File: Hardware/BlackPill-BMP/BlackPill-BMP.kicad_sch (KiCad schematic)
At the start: 27 parts, among them J1 VCC, J2 VCC, J3 Conn_01x10, J4 Conn_01x11, J5 GDB_COMM, J6 VCC, J7 GND, J8 JTAG, J9 LogicAna, U1 STM32F411 BlackPill

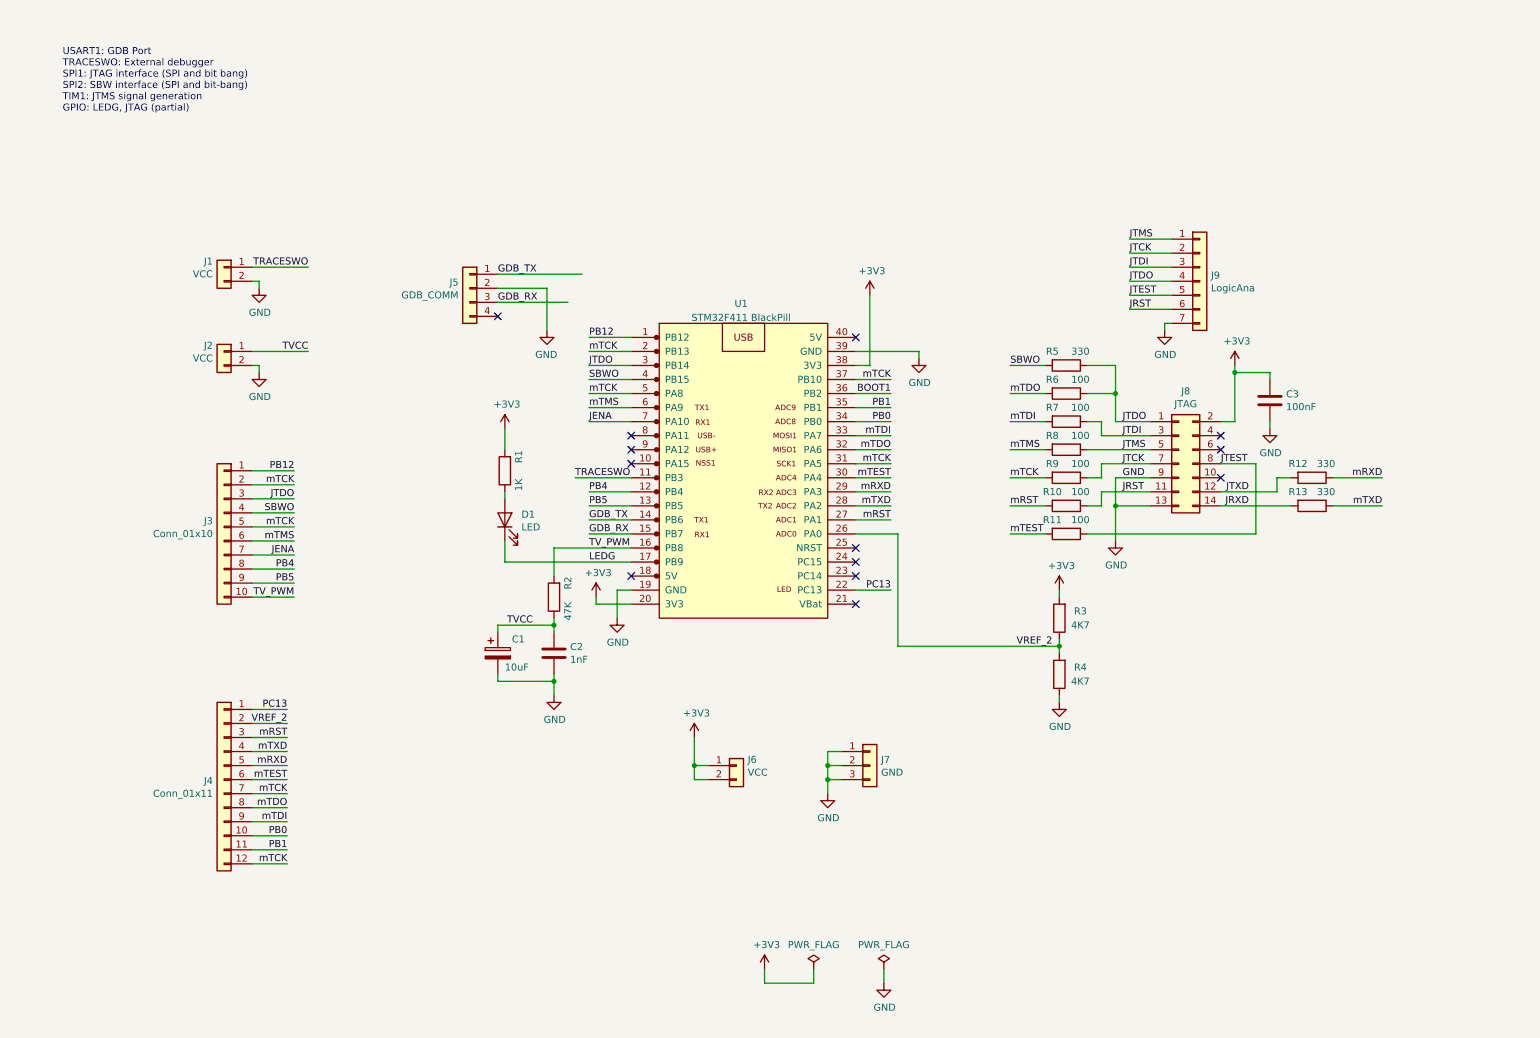
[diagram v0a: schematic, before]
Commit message: Improved BlackPill Board to support both BluePill and BlackPill. Support for variable target voltage.
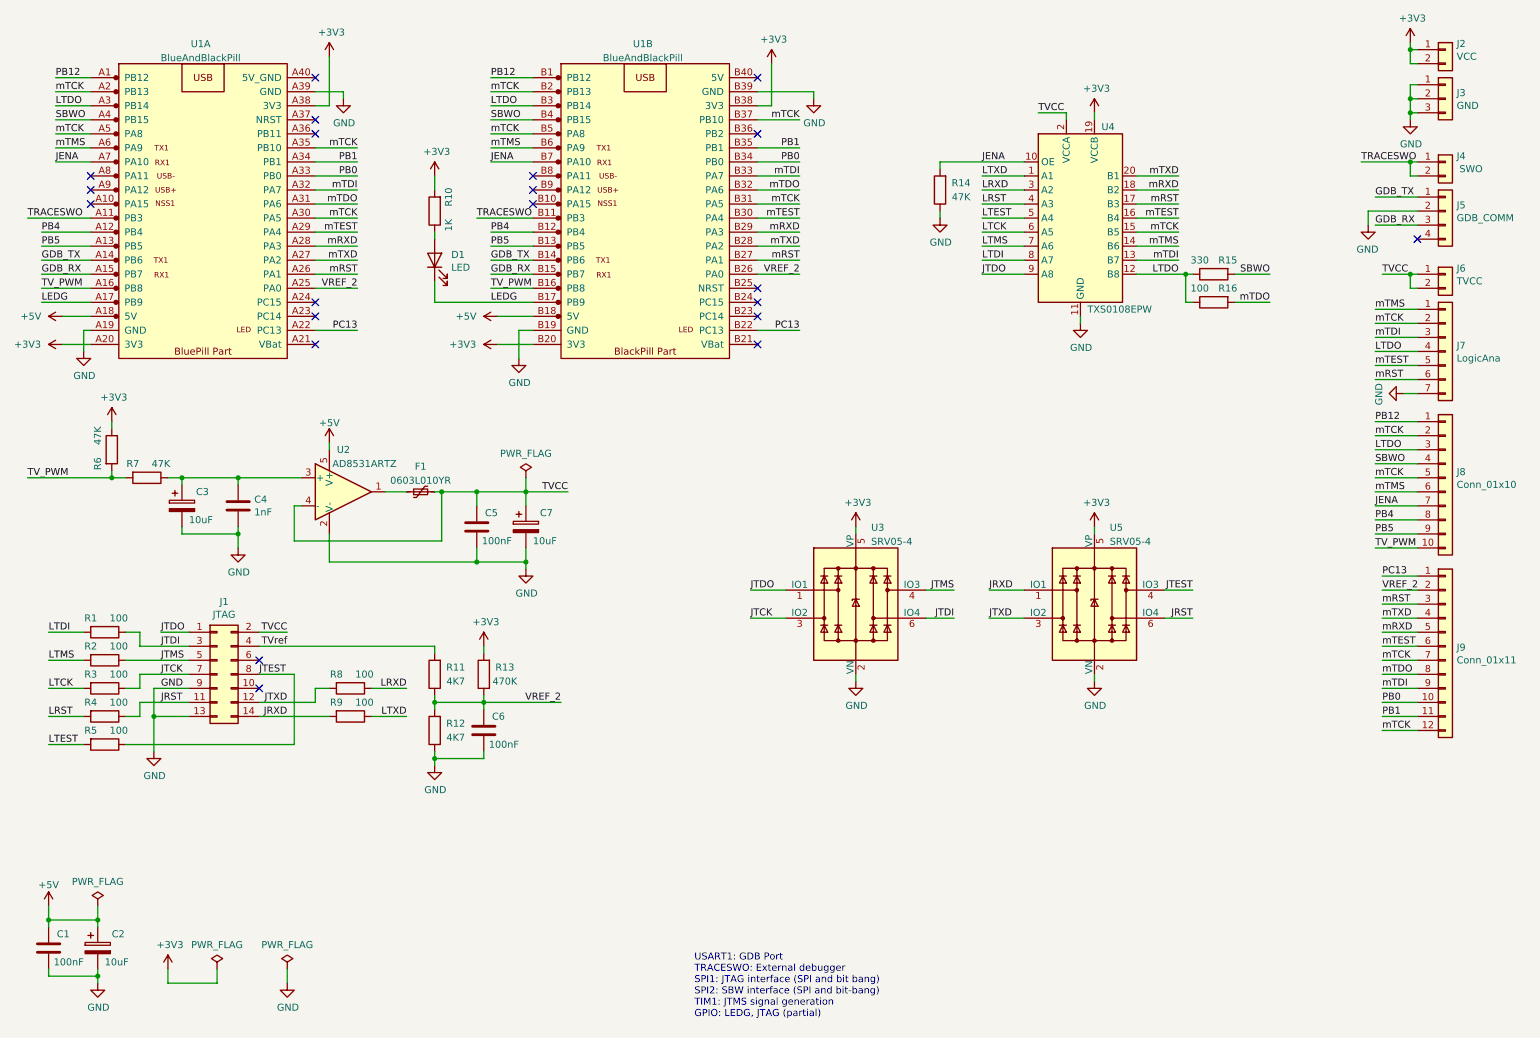
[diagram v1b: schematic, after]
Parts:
- removed U1: STM32F411 BlackPill, lib:BlackPill_F411, symbol BlackPill_F411:BlackPill_F411
- added C1, C6: 100nF, Capacitor_SMD:C_0603_1608Metric_Pad1.08x0.95mm_HandSolder, symbol Device:C
- added C2, C7: 10uF, Capacitor_SMD:C_0603_1608Metric_Pad1.08x0.95mm_HandSolder, symbol Device:C_Polarized
- added F1: 0603L010YR, Fuse:Fuse_0603_1608Metric_Pad1.05x0.95mm_HandSolder, symbol Device:Polyfuse_Small
- added R13: 470K, Resistor_SMD:R_0603_1608Metric_Pad0.98x0.95mm_HandSolder, symbol Device:R
- added R14, R6: 47K, Resistor_SMD:R_0603_1608Metric_Pad0.98x0.95mm_HandSolder, symbol Device:R
- added U1: BlueAndBlackPill, lib:BlueBlackPill, symbol BlueBlackPill:BlueAndBlackPill
- added U2: AD8531ARTZ, Package_TO_SOT_SMD:SOT-23-5_HandSoldering, symbol ad8531artz:AD8531ARTZ
- added U3, U5: SRV05-4, Package_TO_SOT_SMD:SOT-23-6, symbol Power_Protection:SRV05-4
- added U4: TXS0108EPW, Package_SO:TSSOP-20_4.4x6.5mm_P0.65mm, symbol Logic_LevelTranslator:TXS0108EPW
- C3: renamed from C1; footprint Capacitor_THT:CP_Radial_D5.0mm_P2.00mm -> Capacitor_SMD:C_0603_1608Metric_Pad1.08x0.95mm_HandSolder
- C4: renamed from C2; footprint Capacitor_THT:C_Disc_D4.3mm_W1.9mm_P5.00mm -> Capacitor_SMD:C_0603_1608Metric_Pad1.08x0.95mm_HandSolder
- C5: renamed from C3; footprint Capacitor_THT:C_Disc_D4.3mm_W1.9mm_P5.00mm -> Capacitor_SMD:C_0603_1608Metric_Pad1.08x0.95mm_HandSolder
- J4: renamed from J1; value VCC -> SWO
- J6: renamed from J2; value VCC -> TVCC
- R1: renamed from R7; footprint Resistor_THT:R_Axial_DIN0204_L3.6mm_D1.6mm_P7.62mm_Horizontal -> Resistor_SMD:R_0603_1608Metric_Pad0.98x0.95mm_HandSolder
- R10: renamed from R1; footprint Resistor_THT:R_Axial_DIN0204_L3.6mm_D1.6mm_P7.62mm_Horizontal -> Resistor_SMD:R_0603_1608Metric_Pad0.98x0.95mm_HandSolder
- R11: renamed from R3; footprint Resistor_THT:R_Axial_DIN0204_L3.6mm_D1.6mm_P7.62mm_Horizontal -> Resistor_SMD:R_0603_1608Metric_Pad0.98x0.95mm_HandSolder
- R12: renamed from R4; footprint Resistor_THT:R_Axial_DIN0204_L3.6mm_D1.6mm_P7.62mm_Horizontal -> Resistor_SMD:R_0603_1608Metric_Pad0.98x0.95mm_HandSolder
- R15: renamed from R5; footprint Resistor_THT:R_Axial_DIN0204_L3.6mm_D1.6mm_P7.62mm_Horizontal -> Resistor_SMD:R_0603_1608Metric_Pad0.98x0.95mm_HandSolder
- R16: renamed from R6; footprint Resistor_THT:R_Axial_DIN0204_L3.6mm_D1.6mm_P7.62mm_Horizontal -> Resistor_SMD:R_0603_1608Metric_Pad0.98x0.95mm_HandSolder
- R2: renamed from R8; footprint Resistor_THT:R_Axial_DIN0204_L3.6mm_D1.6mm_P7.62mm_Horizontal -> Resistor_SMD:R_0603_1608Metric_Pad0.98x0.95mm_HandSolder
- R3: renamed from R9; footprint Resistor_THT:R_Axial_DIN0204_L3.6mm_D1.6mm_P7.62mm_Horizontal -> Resistor_SMD:R_0603_1608Metric_Pad0.98x0.95mm_HandSolder
- R4: renamed from R10; footprint Resistor_THT:R_Axial_DIN0204_L3.6mm_D1.6mm_P7.62mm_Horizontal -> Resistor_SMD:R_0603_1608Metric_Pad0.98x0.95mm_HandSolder
- R5: renamed from R11; footprint Resistor_THT:R_Axial_DIN0204_L3.6mm_D1.6mm_P7.62mm_Horizontal -> Resistor_SMD:R_0603_1608Metric_Pad0.98x0.95mm_HandSolder
- R7: renamed from R2; footprint Resistor_THT:R_Axial_DIN0204_L3.6mm_D1.6mm_P7.62mm_Horizontal -> Resistor_SMD:R_0603_1608Metric_Pad0.98x0.95mm_HandSolder
- R8: renamed from R12; value 330 -> 100; footprint Resistor_THT:R_Axial_DIN0204_L3.6mm_D1.6mm_P7.62mm_Horizontal -> Resistor_SMD:R_0603_1608Metric_Pad0.98x0.95mm_HandSolder
- R9: renamed from R13; value 330 -> 100; footprint Resistor_THT:R_Axial_DIN0204_L3.6mm_D1.6mm_P7.62mm_Horizontal -> Resistor_SMD:R_0603_1608Metric_Pad0.98x0.95mm_HandSolder
- renumbered J8 to J1, J6 to J2, J7 to J3, J9 to J7, J3 to J8, J4 to J9
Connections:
- net +3V3: now also R13.2, R6.1, U1.A20 (3V3), U1.A38 (3V3), U1.B20 (3V3), U1.B38 (3V3), U3.5 (VP), U4.19 (VCCB), U5.5 (VP); no longer C5.1, J1.2 (Pin_2), R11.2
- net GDB_RX: now also U1.A15 (PB7), U1.B15 (PB7)
- net GDB_TX: now also U1.A14 (PB6), U1.B14 (PB6)
- net GND: now also C5.1, C1.1, C2.2, C6.1, C7.2, R14.1, U1.A19 (GND), U1.A39 (GND), U1.B19 (GND), U1.B39 (GND), U2.2 (V-), U3.2 (VN), U4.11 (GND), U5.2 (VN); no longer C5.2, J4.2 (Pin_2), J6.2 (Pin_2)
- net JENA: now also R14.2, U1.A7 (PA10), U1.B7 (PA10), U4.10 (OE)
- net JRST: now also U5.6 (IO4); no longer J7.6 (Pin_6)
- net JRXD: now also U5.1 (IO1)
- net JTCK: now also U3.3 (IO2); no longer J7.2 (Pin_2)
- net JTDI: now also U3.6 (IO4); no longer J7.3 (Pin_3)
- net JTDO: now also U3.1 (IO1), U4.9 (A8); no longer J7.4 (Pin_4), J8.3 (Pin_3), R15.1, R16.1
- net JTEST: now also U5.4 (IO3); no longer J7.5 (Pin_5)
- net JTMS: now also U3.4 (IO3); no longer J7.1 (Pin_1)
- net JTXD: now also U5.3 (IO2)
- net LEDG: now also U1.A17 (PB9), U1.B17 (PB9)
- net PB0: now also U1.A33 (PB0), U1.B34 (PB0)
- net PB1: now also U1.A34 (PB1), U1.B35 (PB1)
- net PB12: now also U1.A1 (PB12), U1.B1 (PB12)
- net PB4: now also U1.A12 (PB4), U1.B12 (PB4)
- net PB5: now also U1.A13 (PB5), U1.B13 (PB5)
- net PC13: now also U1.A22 (PC13), U1.B22 (PC13)
- net SBWO: now also U1.A4 (PB15), U1.B4 (PB15)
- net TRACESWO: now also J4.2 (Pin_2), U1.A11 (PB3), U1.B11 (PB3)
- net TVCC: now also C5.2, J1.2 (Pin_2), J6.2 (Pin_2), C7.1, F1.2, U2.4 (-), U4.2 (VCCA); no longer C3.1, C4.1, R7.1
- net TV_PWM: now also R6.2, U1.A16 (PB8), U1.B16 (PB8)
- net VREF_2: now also C6.2, R13.1, U1.A25 (PA0), U1.B26 (PA0)
- net mRST: now also J7.6 (Pin_6), U1.A26 (PA1), U1.B27 (PA1), U4.17 (B3); no longer R4.2
- net mRXD: now also U1.A28 (PA3), U1.B29 (PA3), U4.18 (B2); no longer R8.1
- net mTCK: now also J7.2 (Pin_2), U1.A2 (PB13), U1.A30 (PA5), U1.A35 (PB10), U1.A5 (PA8), U1.B2 (PB13), U1.B31 (PA5), U1.B37 (PB10), U1.B5 (PA8), U4.15 (B5); no longer R3.2
- net mTDI: now also J7.3 (Pin_3), U1.A32 (PA7), U1.B33 (PA7), U4.13 (B7); no longer R1.2
- net mTDO: now also U1.A31 (PA6), U1.B32 (PA6)
- net mTEST: now also J7.5 (Pin_5), U1.A29 (PA4), U1.B30 (PA4), U4.16 (B4); no longer R5.2
- net mTMS: now also J7.1 (Pin_1), U1.A6 (PA9), U1.B6 (PA9), U4.14 (B6); no longer R2.2
- net mTXD: now also U1.A27 (PA2), U1.B28 (PA2), U4.20 (B1); no longer R9.1
- net TVref: now reaches J1.4 (Pin_4)
- net TVref: now also R11.2
- new net: C3.1, C4.1, R7.1, U2.3 (+)
- new net: F1.1, U2.1
- new net +5V: C1.2, C2.1, U1.A18 (5V), U1.B18 (5V), U2.5 (V+)
- new net LRST: R4.2, U4.4 (A3)
- new net LRXD: R8.1, U4.3 (A2)
- new net LTCK: R3.2, U4.6 (A5)
- new net LTDI: R1.2, U4.8 (A7)
- new net LTDO: J7.4 (Pin_4), J8.3 (Pin_3), R15.1, R16.1, U1.A3 (PB14), U1.B3 (PB14), U4.12 (B8)
- new net LTEST: R5.2, U4.5 (A4)
- new net LTMS: R2.2, U4.7 (A6)
- new net LTXD: R9.1, U4.1 (A1)
- no-connect marks 13 -> 21
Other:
- moved on the sheet: C3, C4, C5, D1, J1, J2, J3, J4, J5, J6, J7, J8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
